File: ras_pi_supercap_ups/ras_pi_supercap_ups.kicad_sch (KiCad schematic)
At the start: 69 parts

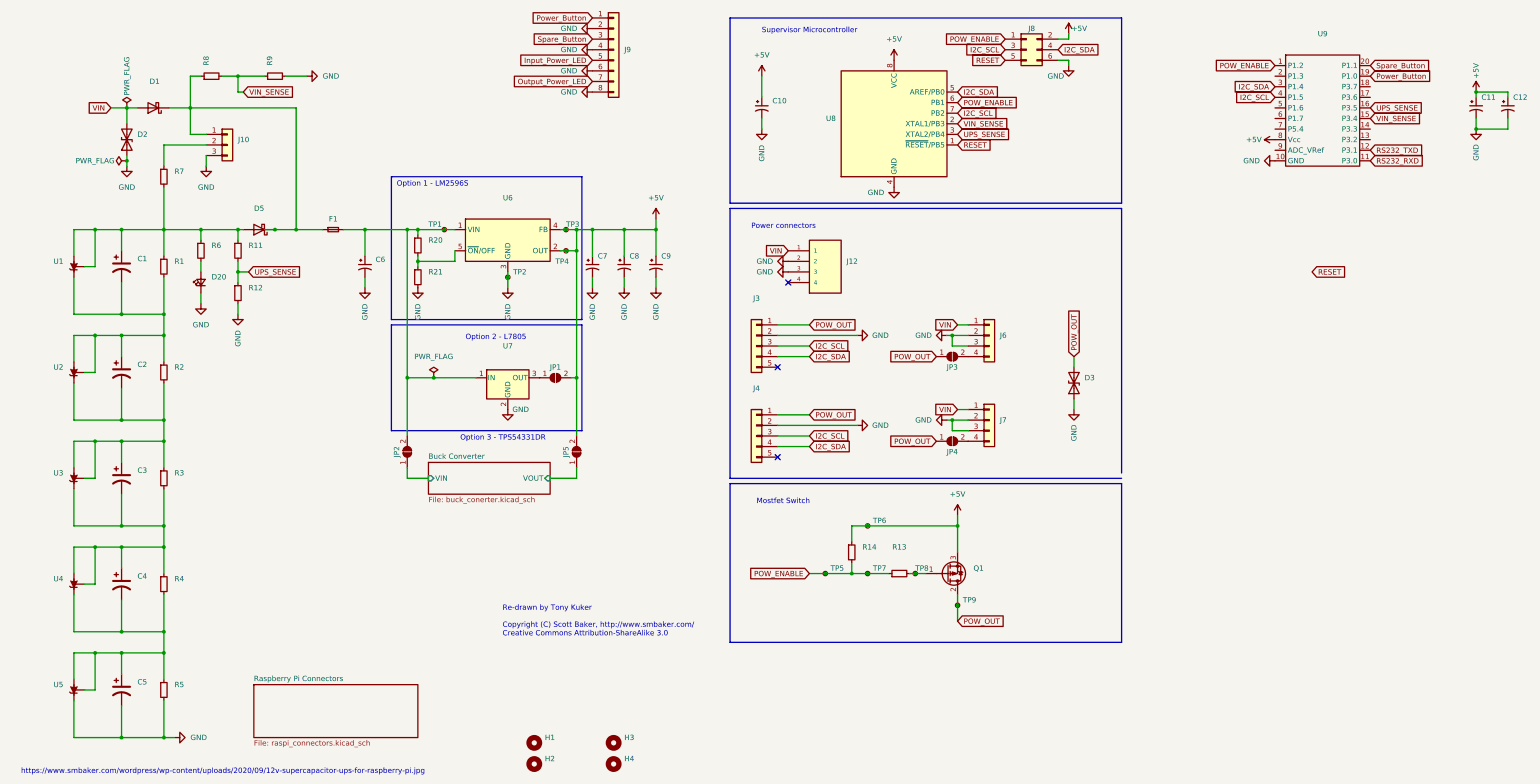
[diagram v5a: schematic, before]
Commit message: updated layout
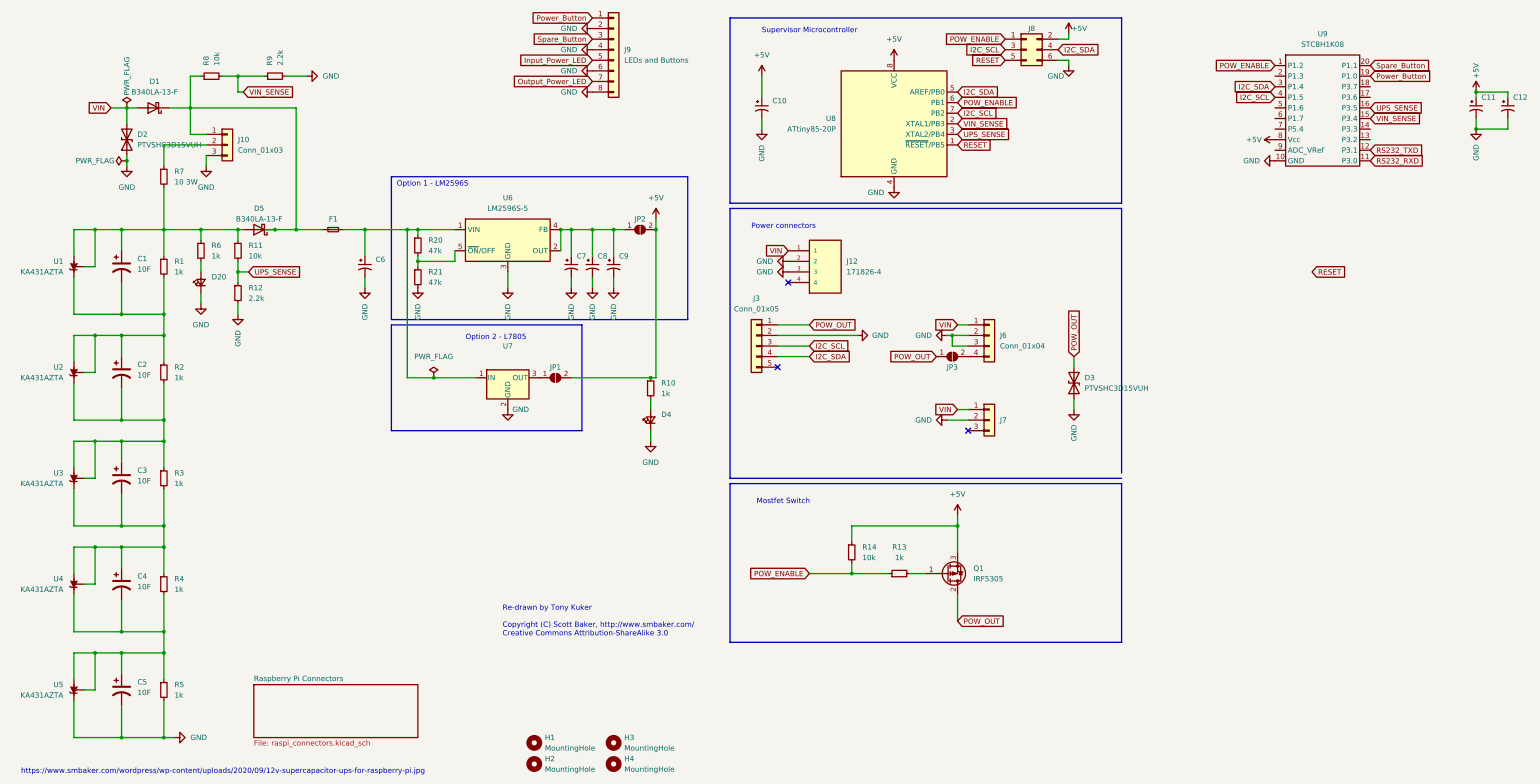
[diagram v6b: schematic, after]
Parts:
- removed J4: (no value), symbol Connector_Generic:Conn_01x05
- removed JP4, JP5: (no value), symbol Jumper:SolderJumper_2_Open
- removed TP1, TP2, TP3, TP4, TP5, TP6, TP7, TP8, TP9: (no value), symbol Connector:TestPoint_Small
- added D4: Green, LED_SMD:LED_0805_2012Metric, symbol Device:LED_Small
- added R10: 1k, Resistor_SMD:R_0805_2012Metric, symbol Device:R_Small
- C1, C2, C3, C4, C5: value (none) -> 10F; footprint (none) -> Capacitor_THT:CP_Radial_D12.5mm_P5.00mm
- C10, C11, C7, C8, C9: value (none) -> 22u 10V X7R; footprint (none) -> Capacitor_SMD:C_0805_2012Metric
- C12: value (none) -> 0.1u; footprint (none) -> Capacitor_SMD:C_0805_2012Metric
- C6: value (none) -> 10u 25V X7R; footprint (none) -> Capacitor_SMD:C_0805_2012Metric
- D1, D5: value (none) -> B340LA-13-F; footprint (none) -> Diode_SMD:D_SMA
- D2, D3: value (none) -> PTVSHC3D15VUH; footprint (none) -> Diode_SMD:D_SOD-323
- D20: value (none) -> Green; footprint (none) -> LED_SMD:LED_0805_2012Metric
- F1: value (none) -> Fuse_Small; footprint (none) -> Fuse:Fuse_1206_3216Metric
- H1, H2, H3, H4: value (none) -> MountingHole; footprint (none) -> MountingHole:MountingHole_2.7mm_M2.5
- J10: value (none) -> Conn_01x03; footprint (none) -> Connector_PinHeader_2.54mm:PinHeader_1x03_P2.54mm_Vertical
- J12: value (none) -> 171826-4; footprint (none) -> TE_171826-4
- J3: value (none) -> Conn_01x05; footprint (none) -> Connector_PinHeader_2.54mm:PinHeader_1x05_P2.54mm_Vertical
- J6: value (none) -> Conn_01x04; footprint (none) -> Connector_PinHeader_2.54mm:PinHeader_1x04_P2.54mm_Vertical
- J7: symbol Connector_Generic:Conn_01x04 -> Connector_Generic:Conn_01x03
- J8: value (none) -> Conn_02x03_Odd_Even; footprint (none) -> Connector_PinHeader_2.54mm:PinHeader_2x03_P2.54mm_Vertical
- J9: value (none) -> LEDs and Buttons; footprint (none) -> Connector_PinHeader_2.54mm:PinHeader_1x08_P2.54mm_Vertical
- JP1, JP2, JP3: value (none) -> SolderJumper_2_Open; footprint (none) -> Jumper:SolderJumper-2_P1.3mm_Open_RoundedPad1.0x1.5mm
- Q1: value (none) -> IRF5305; footprint (none) -> Package_TO_SOT_SMD:TO-263-2
- R1, R2, R3, R4, R5: value (none) -> 1k; footprint (none) -> Resistor_SMD:R_1206_3216Metric
- R11, R14, R8: value (none) -> 10k; footprint (none) -> Resistor_SMD:R_0805_2012Metric
- R12, R9: value (none) -> 2.2k; footprint (none) -> Resistor_SMD:R_0805_2012Metric
- R13, R6: value (none) -> 1k; footprint (none) -> Resistor_SMD:R_0805_2012Metric
- R20, R21: value (none) -> 47k; footprint (none) -> Resistor_SMD:R_0805_2012Metric
- R7: value (none) -> 10 3W; footprint (none) -> Resistor_THT:R_Axial_DIN0516_L15.5mm_D5.0mm_P25.40mm_Horizontal
- U1, U2, U3, U4, U5: value (none) -> KA431AZTA; footprint (none) -> Package_TO_SOT_THT:TO-92_Inline
- U6: value (none) -> LM2596S-5; footprint (none) -> Package_TO_SOT_SMD:TO-263-5_TabPin3
- U8: value (none) -> ATtiny85-20P; footprint (none) -> Package_DIP:DIP-8_W7.62mm
- U9: value (none) -> STC8H1K08; footprint (none) -> Package_SO:TSSOP-20_4.4x5mm_P0.5mm
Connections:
- net +5V: now also JP2.2 (B), R10.1; no longer C7.1, C8.1, C9.1, U6.2 (OUT), U6.4 (FB)
- net GND: now also D4.1 (K); no longer J7.3 (Pin_3)
- net at C6.1, F1.2, R20.1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: no longer JP2.2 (B)
- net Buck Converter/VIN: no longer names the net of JP2.1 (A)
- net Buck Converter/VIN: now also C7.1, C8.1, C9.1, U6.2 (OUT), U6.4 (FB)
- new net: D4.2 (A), R10.2
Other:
- removed sheet Buck Converter
- note removed: "Option 3 - TPS54331DR"
- moved on the sheet: C7, C8, C9

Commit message: As ordered v0.9
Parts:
- added J4: Conn_01x03, Connector_PinHeader_2.54mm:PinHeader_1x03_P2.54mm_Vertical, symbol Connector_Generic:Conn_01x03
- added R15, R16: 1k, Resistor_SMD:R_0805_2012Metric, symbol Device:R_Small
- added TP1: TestPoint_Small, TestPoint:TestPoint_THTPad_D1.0mm_Drill0.5mm, symbol Connector:TestPoint_Small
- C1, C2, C3, C4, C5, H1, H2, H3, H4, J10, J12, J3, J6, J8, JP1, JP2, JP3, R7, U8: LCSC (none) -> DNP
- C10, C11, C7, C8, C9: LCSC (none) -> C45783
- C6: LCSC (none) -> C15850
- F1: LCSC C140540 -> C140470
- J7: value (none) -> Conn_01x03; footprint (none) -> Connector_PinHeader_2.54mm:PinHeader_1x03_P2.54mm_Vertical; LCSC (none) -> DNP
- J9: footprint Connector_PinHeader_2.54mm:PinHeader_1x08_P2.54mm_Vertical -> Connector_PinHeader_2.54mm:PinHeader_1x04_P2.54mm_Vertical; symbol Connector_Generic:Conn_01x08 -> Connector_Generic:Conn_01x04; LCSC (none) -> DNP
- R1, R2, R3, R4, R5: LCSC (none) -> C4410
- R10, R13, R6: LCSC (none) -> C17513
- R11, R14, R8: LCSC (none) -> C17414
- R12, R9: LCSC (none) -> C17520
- R20, R21: LCSC (none) -> C17713
- U1, U2, U3, U4, U5: value KA431AZTA -> KA431SMFTF; footprint Package_TO_SOT_THT:TO-92_Inline -> Package_TO_SOT_SMD:SOT-23; symbol Reference_Voltage:TL431LP -> Reference_Voltage:TL432DBZ; LCSC C124501 -> C232815
- U6: LCSC (none) -> C347421
- U7: value (none) -> L7805; footprint (none) -> Connector_PinSocket_2.54mm:PinSocket_1x03_P2.54mm_Vertical; LCSC (none) -> DNP
- U9: footprint Package_SO:TSSOP-20_4.4x5mm_P0.5mm -> Package_SO:TSSOP-20_4.4x6.5mm_P0.65mm
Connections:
- net +5V: now also R15.1, R16.1
- net GND: now also U5.2 (K), J4.2 (Pin_2); no longer J9.6 (Pin_6), J9.8 (Pin_8), U5.3 (K)
- net I2C_SCL: now also J3.4 (Pin_4); no longer J3.3 (Pin_3)
- net I2C_SDA: now also J3.5 (Pin_5); no longer J3.4 (Pin_4)
- net Power_Button: now also R16.2
- net RS232_RXD: now also J4.1 (Pin_1)
- net RS232_TXD: now also J4.3 (Pin_3)
- net Spare_Button: now also R15.2
- net at C3.2, C4.1, R3.2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: now also U3.2 (K), U4.3 (A); no longer U3.3 (K), U4.2 (A)
- net at C4.2, C5.1, R4.2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: now also U4.2 (K), U5.3 (A); no longer U4.3 (K), U5.2 (A)
- net at C1.1, D5.2 (A), R1.1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: now also U1.3 (A); no longer U1.2 (A)
- net at C1.2, C2.1, R1.2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: now also U1.2 (K), U2.3 (A); no longer U1.3 (K), U2.2 (A)
- net at C2.2, C3.1, R2.2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: now also U2.2 (K), U3.3 (A); no longer U2.3 (K), U3.2 (A)
- net at U9.9 (ADC_VRef): now also TP1.1
- removed net Input_Power_LED: J9.5 (Pin_5)
- removed net Output_Power_LED: J9.7 (Pin_7)
- no-connect marks 3 -> 11
